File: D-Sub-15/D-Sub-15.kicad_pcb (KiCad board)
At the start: 2 copper layers, 99.1 x 53.3 mm, 3 parts, among them J1 Pins, J2 Socket, J3 Breakout

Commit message: Corerect URL.
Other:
- board text added: "D-Sub 15 Breakout Board ©2025 Dieter Baron github.com/T-Pau/Connector-Breakout-Boards"
- board text removed: "D-Sub 15 Breakout Board ©2025 Dieter Baron github.com/T-Pau/Breakout-Boards"

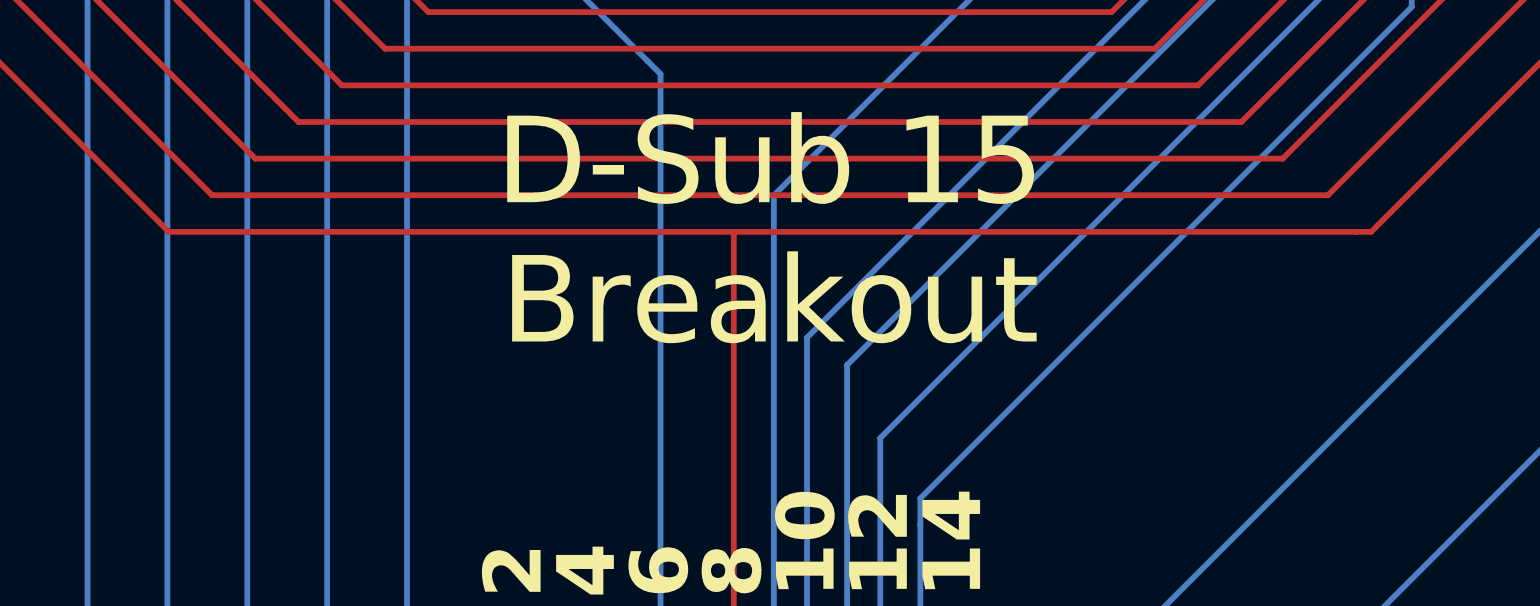
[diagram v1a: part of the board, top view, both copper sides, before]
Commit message: Improve layouts, add DIN-8 270° board.
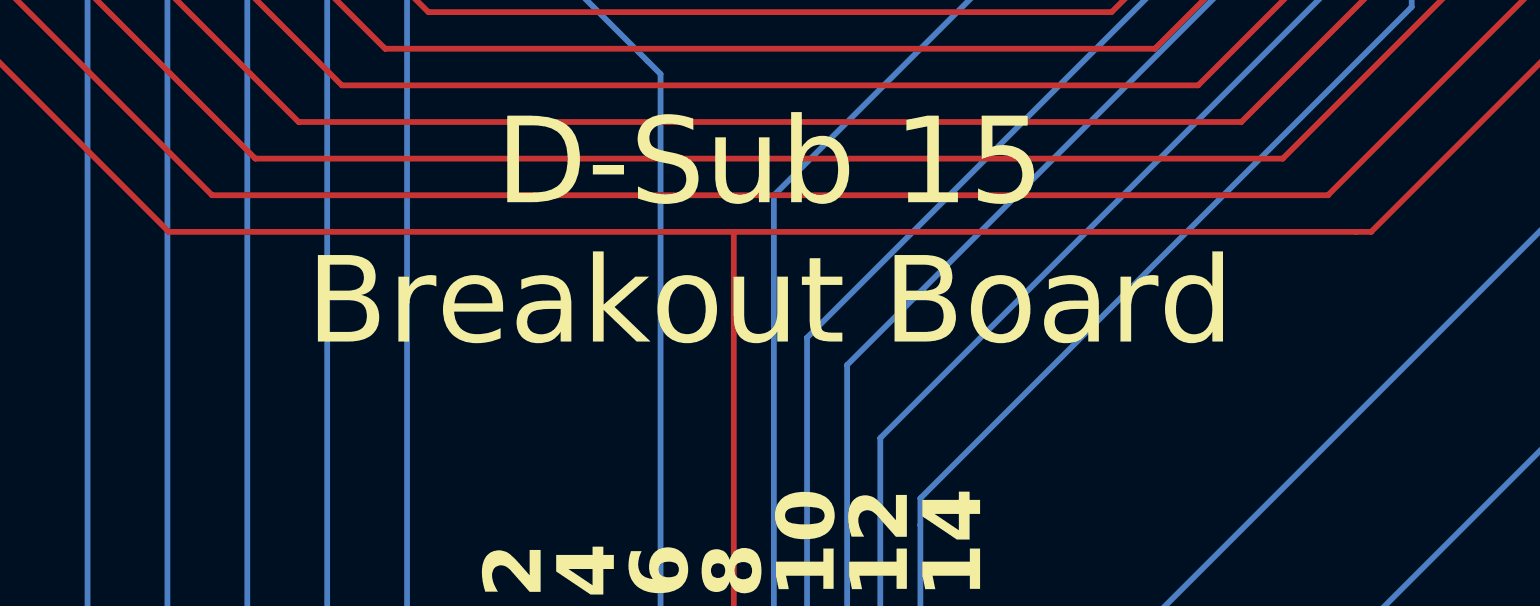
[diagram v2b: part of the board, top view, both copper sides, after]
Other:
- board text added: "D-Sub 15 Breakout Board"
- board text removed: "D-Sub 15 Breakout"

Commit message: Begin SCART breakout board.
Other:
- board text added: "D-Sub 15 Breakout Board Revision 1 ©2025 Dieter Baron github.com/T-Pau/Connector-Breakout-Boards"
- board text removed: "D-Sub 15 Breakout Board ©2025 Dieter Baron github.com/T-Pau/Connector-Breakout-Boards"
